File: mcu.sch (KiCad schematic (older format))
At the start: 19 parts, among them J8 CONN_01X06, J9 CONN_01X03, SW3 SW_Push, U6 STM32L476RG, Y1 ABS07-120-32.768kHz-T

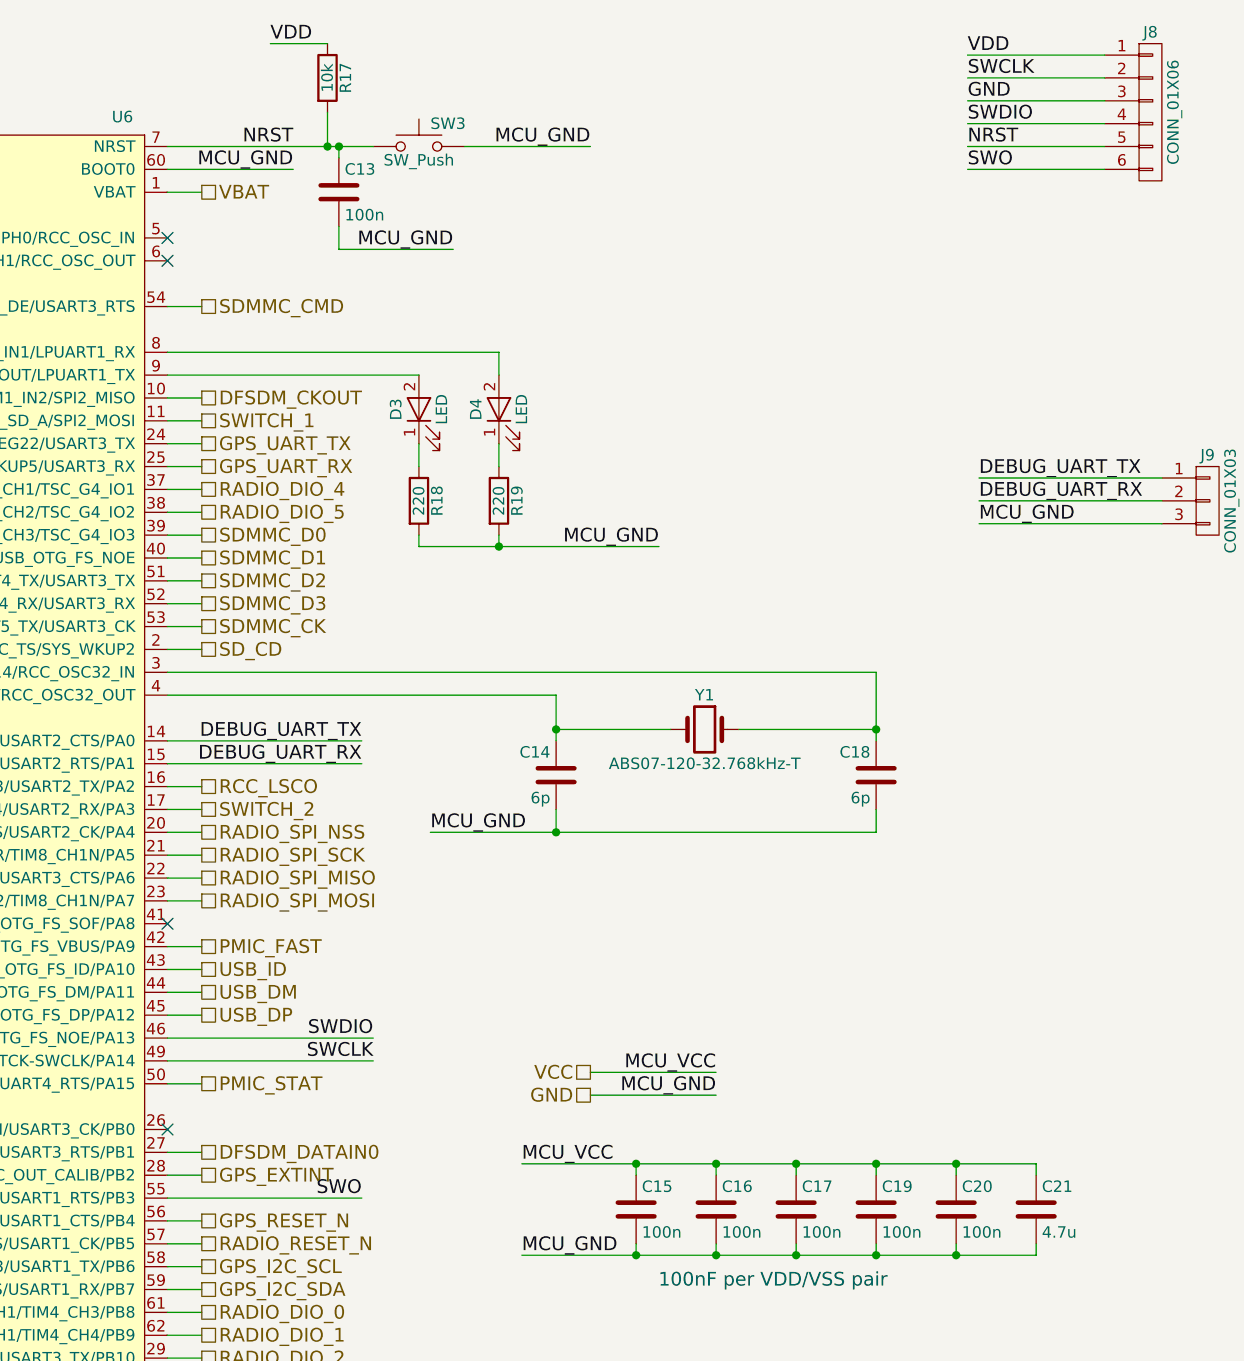
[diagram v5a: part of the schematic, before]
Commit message: Rev 3 DRC clean
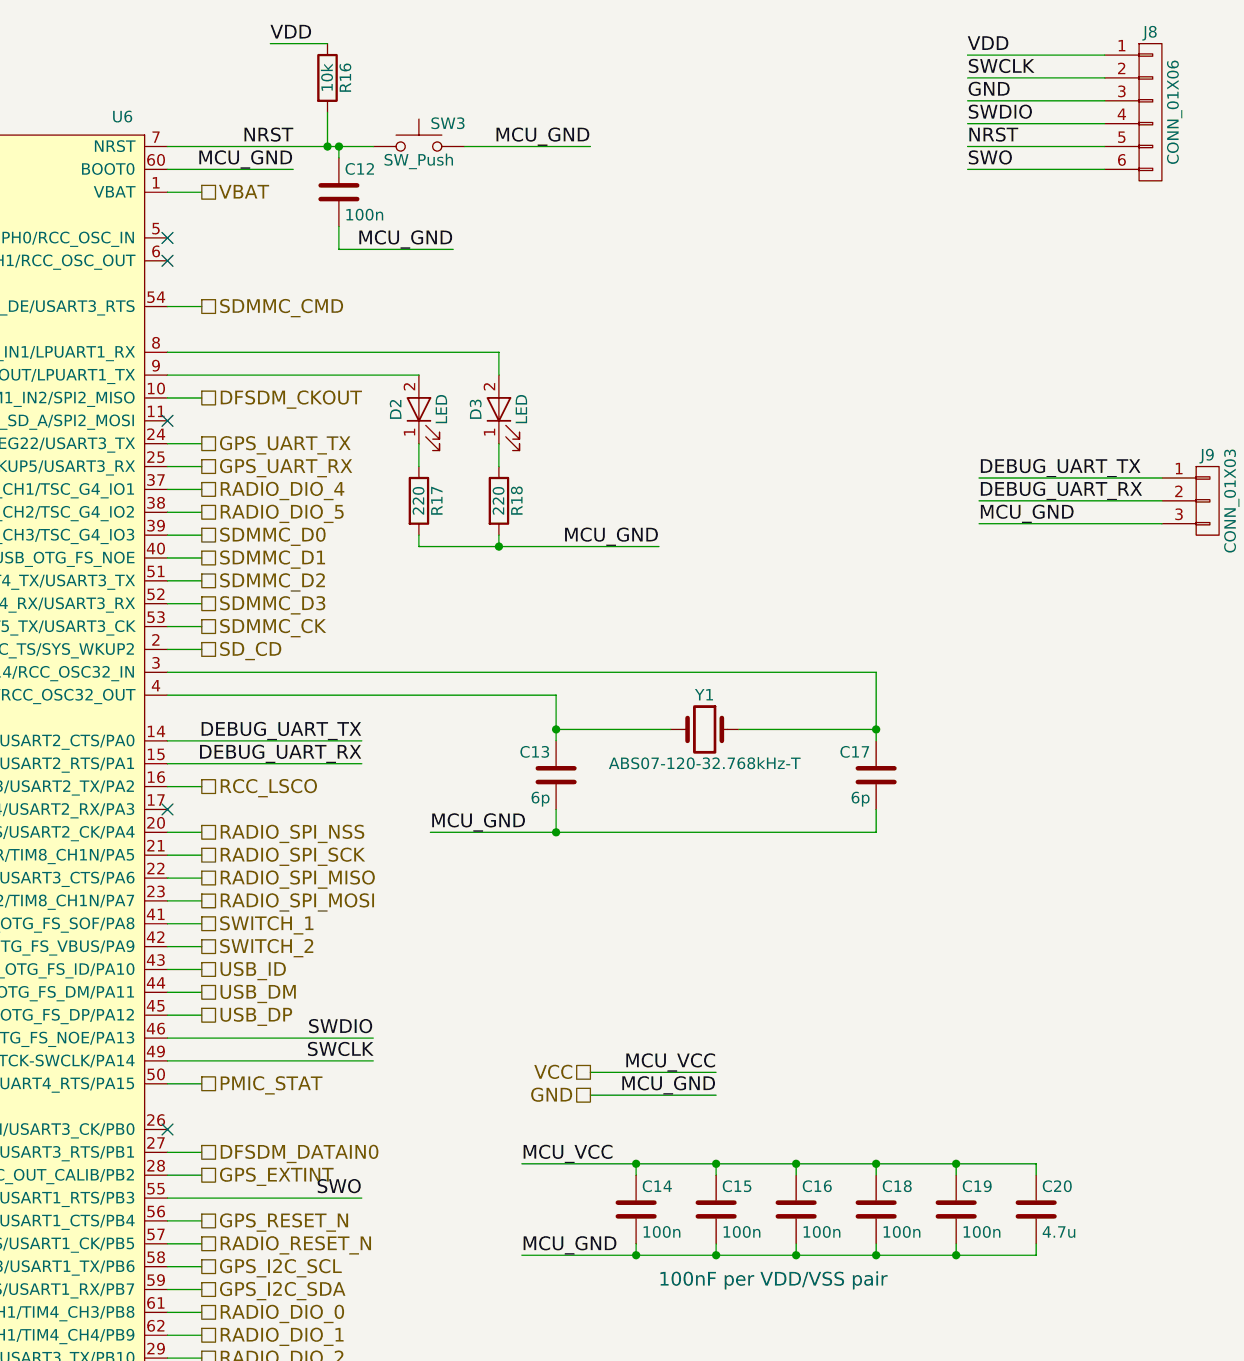
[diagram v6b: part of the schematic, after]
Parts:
- renumbered C13 to C12, C14 to C13, C15 to C14, C16 to C15, C17 to C16, C18 to C17, C19 to C18, C20 to C19, C21 to C20, D3 to D2, D4 to D3, R17 to R16, R18 to R17, R19 to R18
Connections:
- net PMIC_FAST is gone; now on net SWITCH_2: U6.42 (DAC1_EXTI9/LCD_COM1/TIM15_BKIN/TIM1_CH2/USART1_TX/USB_OTG_FS_VBUS/PA9)
- net SWITCH_1: now also U6.41 (LCD_COM0/LPTIM2_OUT/RCC_MCO/TIM1_CH1/USART1_CK/USB_OTG_FS_SOF/PA8); no longer U6.11 (PC3/ADC1_IN4/ADC2_IN4/ADC3_IN4/LCD_VLCD/LPTIM1_ETR/LPTIM2_ETR/SAI1_SD_A/SPI2_MOSI)
- net SWITCH_2: no longer U6.17 (ADC1_IN8/ADC2_IN8/LCD_SEG2/OPAMP1_VOUT/TIM15_CH2/TIM2_CH4/TIM5_CH4/USART2_RX/PA3)
- no-connect marks 6 -> 7
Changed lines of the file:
@@
 DEBUG_UART_RX
 $Comp
-L C C15
+L C C14
 U 1 1 59A77466
 P 9900 6100
-F 0 "C15" H 9925 6200 50  0000 L CNN
+F 0 "C14" H 9925 6200 50  0000 L CNN
 F 1 "100n" H 9925 6000 50  0000 L CNN
 F 2 "Capacitors_SMD:C_0805_HandSoldering" H 9938 5950 50  0001 C CNN
@@
 $EndComp
 $Comp
-L C C14
+L C C13
 U 1 1 59B38E77
 P 9550 4200
-F 0 "C14" H 9575 4300 50  0000 L CNN
+F 0 "C13" H 9575 4300 50  0000 L CNN
 F 1 "6p" H 9575 4100 50  0000 L CNN
 F 2 "Capacitors_SMD:C_0805_HandSoldering" H 9588 4050 50  0001 C CNN
@@
 100nF per VDD/VSS pair
 $Comp
-L C C21
+L C C20
 U 1 1 59BF0662
 P 11650 6100
-F 0 "C21" H 11675 6200 50  0000 L CNN
+F 0 "C20" H 11675 6200 50  0000 L CNN
 F 1 "4.7u" H 11675 6000 50  0000 L CNN
 F 2 "Capacitors_SMD:C_0805_HandSoldering" H 11688 5950 50  0001 C CNN
@@
 	8000 4250 7850 4250
 $Comp
-L LED D3
+L LED D2
 U 1 1 59BF17F5
 P 8950 2600
-F 0 "D3" H 8950 2700 50  0000 C CNN
+F 0 "D2" H 8950 2700 50  0000 C CNN
 F 1 "LED" H 8950 2500 50  0000 C CNN
 F 2 "LEDs:LED_0805_HandSoldering" H 8950 2600 50  0001 C CNN
@@
 $EndComp
 $Comp
-L R R19
+L R R18
 U 1 1 59BF19BB
 P 9300 3000
-F 0 "R19" V 9380 3000 50  0000 C CNN
+F 0 "R18" V 9380 3000 50  0000 C CNN
 F 1 "220" V 9300 3000 50  0000 C CNN
 F 2 "Resistors_SMD:R_0805_HandSoldering" V 9230 3000 50  0001 C CNN
@@
 	10950 4450 10950 4350
 $Comp
-L R R18
+L R R17
 U 1 1 59C07A6F
 P 8950 3000
-F 0 "R18" V 9030 3000 50  0000 C CNN
+F 0 "R17" V 9030 3000 50  0000 C CNN
 F 1 "220" V 8950 3000 50  0000 C CNN
 F 2 "Resistors_SMD:R_0805_HandSoldering" V 8880 3000 50  0001 C CNN
@@
 	11400 2900 12200 2900
 $Comp
-L C C18
+L C C17
 U 1 1 59C089D0
 P 10950 4200
-F 0 "C18" H 10975 4300 50  0000 L CNN
+F 0 "C17" H 10975 4300 50  0000 L CNN
 F 1 "6p" H 10975 4100 50  0000 L CNN
 F 2 "Capacitors_SMD:C_0805_HandSoldering" H 10988 4050 50  0001 C CNN
@@
 $EndComp
 $Comp
-L C C16
+L C C15
 U 1 1 59C09613
 P 10250 6100
-F 0 "C16" H 10275 6200 50  0000 L CNN
+F 0 "C15" H 10275 6200 50  0000 L CNN
 F 1 "100n" H 10275 6000 50  0000 L CNN
 F 2 "Capacitors_SMD:C_0805_HandSoldering" H 10288 5950 50  0001 C CNN
@@
 $EndComp
 $Comp
-L C C17
+L C C16
 U 1 1 59C09660
 P 10600 6100
-F 0 "C17" H 10625 6200 50  0000 L CNN
+F 0 "C16" H 10625 6200 50  0000 L CNN
 F 1 "100n" H 10625 6000 50  0000 L CNN
 F 2 "Capacitors_SMD:C_0805_HandSoldering" H 10638 5950 50  0001 C CNN
@@
 $EndComp
 $Comp
-L C C19
+L C C18
 U 1 1 59C096AC
 P 10950 6100
-F 0 "C19" H 10975 6200 50  0000 L CNN
+F 0 "C18" H 10975 6200 50  0000 L CNN
 F 1 "100n" H 10975 6000 50  0000 L CNN
 F 2 "Capacitors_SMD:C_0805_HandSoldering" H 10988 5950 50  0001 C CNN
@@
 $EndComp
 $Comp
-L C C20
+L C C19
 U 1 1 59C096FD
 P 11300 6100
-F 0 "C20" H 11325 6200 50  0000 L CNN
+F 0 "C19" H 11325 6200 50  0000 L CNN
 F 1 "100n" H 11325 6000 50  0000 L CNN
 F 2 "Capacitors_SMD:C_0805_HandSoldering" H 11338 5950 50  0001 C CNN
@@
 $EndComp
 $Comp
-L LED D4
+L LED D3
 U 1 1 59C09B57
 P 9300 2600
-F 0 "D4" H 9300 2700 50  0000 C CNN
+F 0 "D3" H 9300 2700 50  0000 C CNN
 F 1 "LED" H 9300 2500 50  0000 C CNN
 F 2 "LEDs:LED_0805_HandSoldering" H 9300 2600 50  0001 C CNN
@@
 Text HLabel 8000 5550 2    60   UnSpc ~ 0
 PMIC_STAT
-Text HLabel 8000 4950 2    60   UnSpc ~ 0
-PMIC_FAST
 Wire Wire Line
 	8000 5550 7850 5550
@@
 Wire Wire Line
 	10250 5600 9700 5600
-Text HLabel 8000 2650 2    60   UnSpc ~ 0
+Text HLabel 8000 4850 2    60   UnSpc ~ 0
 SWITCH_1
-Text HLabel 8000 4350 2    60   UnSpc ~ 0
+Text HLabel 8000 4950 2    60   UnSpc ~ 0
 SWITCH_2
 $Comp
@@
 	-1   0    0    -1
 $EndComp
-Wire Wire Line
-	8000 4350 7850 4350
-NoConn ~ 7850 4850
-Wire Wire Line
-	7850 2650 8000 2650
 Text HLabel 8000 6950 2    60   UnSpc ~ 0
 VUSB_DET
@@
 NoConn ~ 7850 5750
 $Comp
-L R R17
+L R R16
 U 1 1 5ACBFB3F
 P 8550 1150
-F 0 "R17" V 8630 1150 50  0000 C CNN
+F 0 "R16" V 8630 1150 50  0000 C CNN
 F 1 "10k" V 8550 1150 50  0000 C CNN
 F 2 "Resistors_SMD:R_0805_HandSoldering" V 8480 1150 50  0001 C CNN
@@
 $EndComp
 $Comp
-L C C13
+L C C12
 U 1 1 5ACBFBD9
 P 8600 1650
-F 0 "C13" H 8625 1750 50  0000 L CNN
+F 0 "C12" H 8625 1750 50  0000 L CNN
 F 1 "100n" H 8625 1550 50  0000 L CNN
 F 2 "Capacitors_SMD:C_0805_HandSoldering" H 8638 1500 50  0001 C CNN
@@
 Wire Wire Line
 	8600 1900 8600 1800
+Wire Wire Line
+	7850 4850 8000 4850
+NoConn ~ 7850 2650
+NoConn ~ 7850 4350
 $EndSCHEMATC
